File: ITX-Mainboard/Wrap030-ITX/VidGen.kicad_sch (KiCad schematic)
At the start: 26 parts, among them J3 DE15_Receptacle_HighDensity_M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, X2 25.175M

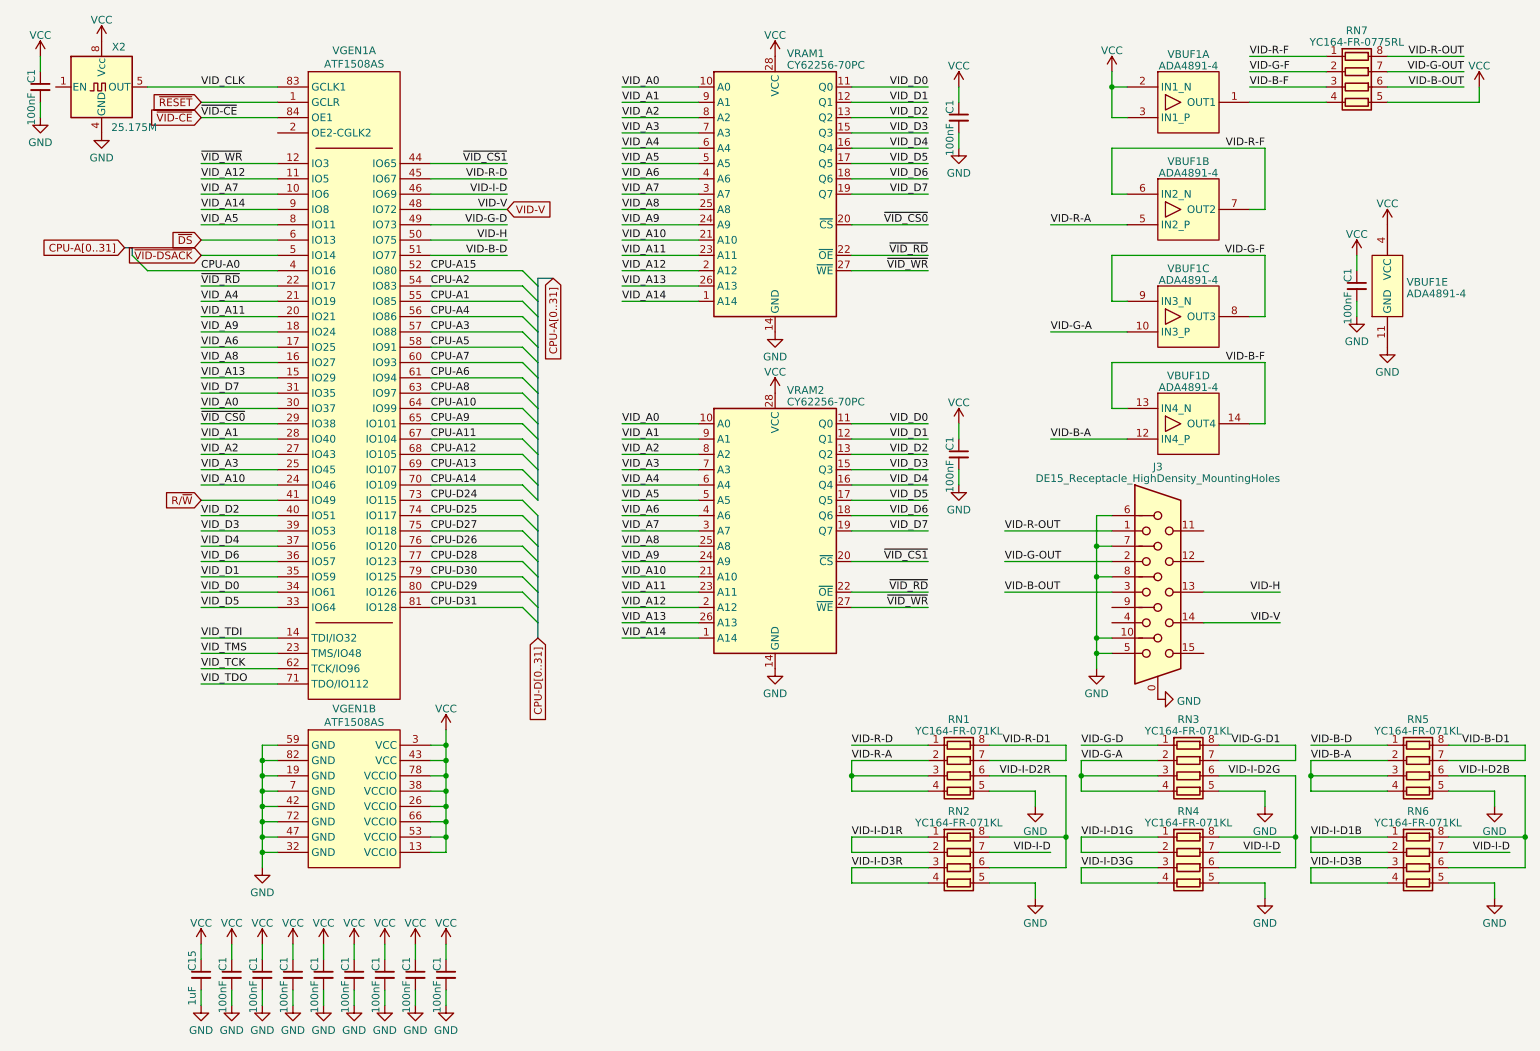
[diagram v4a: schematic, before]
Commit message: Replace resistor nets with 0402 & update gerbers
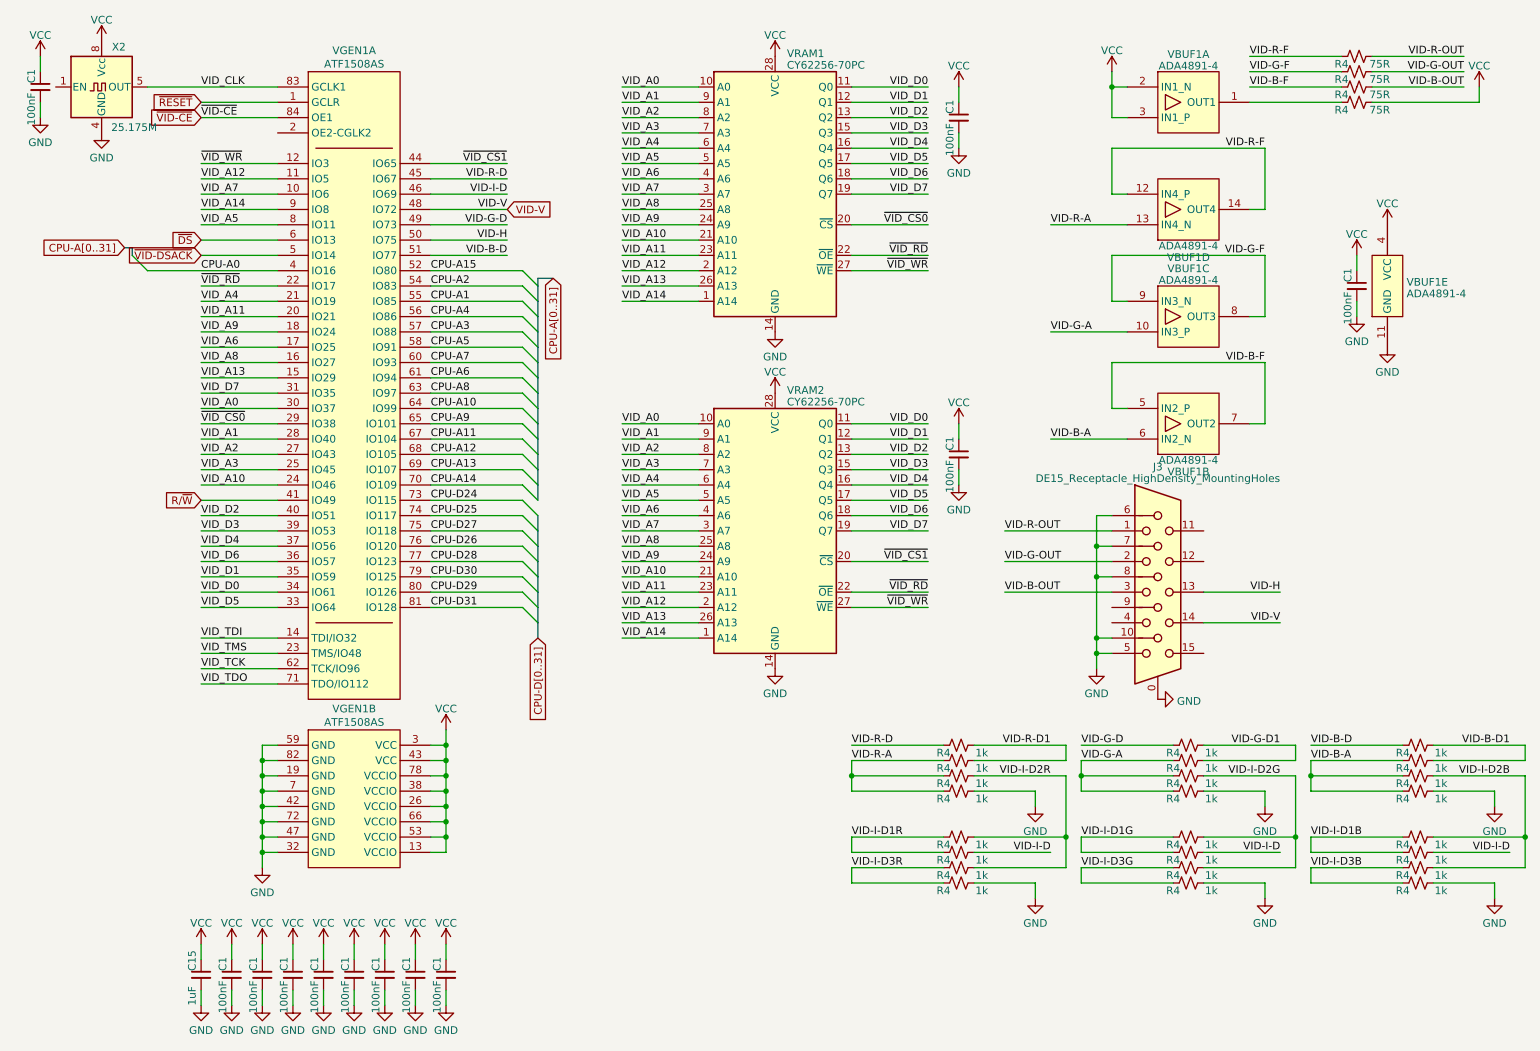
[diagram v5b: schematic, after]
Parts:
- removed RN1, RN2, RN3, RN4, RN5, RN6: YC164-FR-071KL, Resistor_SMD:R_Array_Convex_4x1206, symbol Device:R_Pack04
- removed RN7: YC164-FR-0775RL, Resistor_SMD:R_Array_Convex_4x1206, symbol Device:R_Pack04
- added R4 (x24): 1k, Resistor_SMD:R_0402_1005Metric_Pad0.72x0.64mm_HandSolder, symbol Device:R_Small_US
- added R4 (x4): 75R, Resistor_SMD:R_0402_1005Metric_Pad0.72x0.64mm_HandSolder, symbol Device:R_Small_US
- C1: Mouser-Part (none) -> 187-CL05B104KO5NNNC; Notes (none) -> JLC
- C15: Mouser-Part (none) -> 187-CL05A105KA5NQNC; Notes (none) -> JLC
- J3: Notes (none) -> Mouser
- VBUF1: Mouser-Part (none) -> 584-ADA4891-4ARZ; Notes (none) -> Mouser
- VGEN1: Mouser-Part (none) -> 556-ATF1508AS-10JU84; Notes (none) -> OFE; Socket-Mouser (none) -> 575-948424
- VRAM1, VRAM2: Mouser-Part (none) -> 972-71256SA15TPG; Notes (none) -> OFE; Socket-Mouser (none) -> 571-1-2199298-9
- X2: Mouser-Part (none) -> 774-MXO45HS-3C-25.1; Notes (none) -> Mouser
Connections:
- net GND: now also R4.2, R4.2, R4.2, R4.2, R4.2, R4.2
- net VCC: now also R4.2
- net VID-B-A: now also VBUF1.6 (IN2_N), R4.1, R4.1, R4.1; no longer VBUF1.12 (IN4_P)
- net VID-B-D: now also R4.1
- net VID-B-D1: now also R4.2, R4.2
- net VID-B-F: now also VBUF1.5 (IN2_P), VBUF1.7 (OUT2), R4.1; no longer VBUF1.13 (IN4_N), VBUF1.14 (OUT4)
- net VID-B-OUT: now also R4.2
- net VID-G-A: now also R4.1, R4.1, R4.1
- net VID-G-D: now also R4.1
- net VID-G-D1: now also R4.2, R4.2
- net VID-G-F: now also R4.1
- net VID-G-OUT: now also R4.2
- net VID-I-D: now also R4.2, R4.2, R4.2
- net VID-I-D1B: now also R4.1, R4.1
- net VID-I-D1G: now also R4.1, R4.1
- net VID-I-D1R: now also R4.1, R4.1
- net VID-I-D2B: now also R4.2, R4.2, R4.2
- net VID-I-D2G: now also R4.2, R4.2, R4.2
- net VID-I-D2R: now also R4.2, R4.2, R4.2
- net VID-I-D3B: now also R4.1, R4.1
- net VID-I-D3G: now also R4.1, R4.1
- net VID-I-D3R: now also R4.1, R4.1
- net VID-R-A: now also VBUF1.13 (IN4_N), R4.1, R4.1, R4.1; no longer VBUF1.5 (IN2_P)
- net VID-R-D: now also R4.1
- net VID-R-D1: now also R4.2, R4.2
- net VID-R-F: now also VBUF1.12 (IN4_P), VBUF1.14 (OUT4), R4.1; no longer VBUF1.6 (IN2_N), VBUF1.7 (OUT2)
- net VID-R-OUT: now also R4.2
- net at VBUF1.1 (OUT1): now also R4.1
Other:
- moved on the sheet: VBUF1B, VBUF1D
